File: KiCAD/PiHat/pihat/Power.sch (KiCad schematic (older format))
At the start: 0 parts

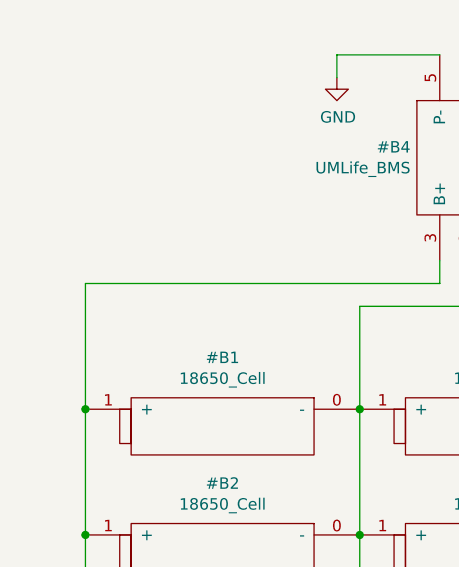
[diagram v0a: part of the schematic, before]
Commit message: Added status LEDs, power relay, organized traces
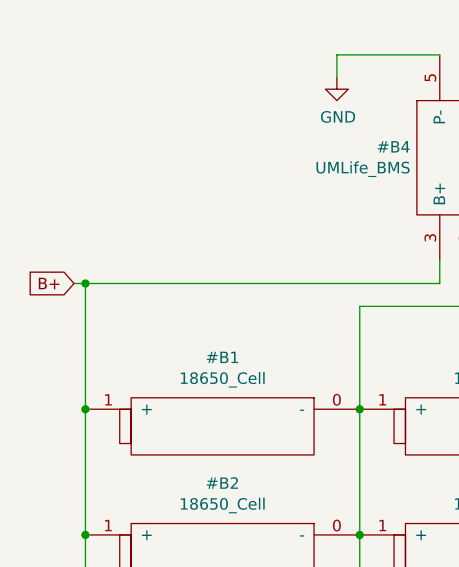
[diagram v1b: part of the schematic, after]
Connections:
- net labels added: B+
- wire segments 34 -> 35
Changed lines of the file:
@@
 EESchema Schematic File Version 4
-LIBS:pihat-cache
 EELAYER 30 0
 EELAYER END
@@
 $EndComp
 $Comp
+L Device:Solar_Cell #SC1
+U 1 1 5E5BBB14
+P 4550 3850
+F 0 "#SC1" H 4383 3946 50  0000 R CNN
+F 1 "Solar_Cell" H 4383 3855 50  0000 R CNN
+F 2 "" V 4550 3910 50  0001 C CNN
+F 3 "~" V 4550 3910 50  0001 C CNN
+	1    4550 3850
+	1    0    0    -1
+$EndComp
+$Comp
+L power:GND #PWR011
+U 1 1 5E5BEAFD
+P 4550 4250
+F 0 "#PWR011" H 4550 4000 50  0001 C CNN
+F 1 "GND" H 4555 4077 50  0000 C CNN
+F 2 "" H 4550 4250 50  0001 C CNN
+F 3 "" H 4550 4250 50  0001 C CNN
+	1    4550 4250
+	1    0    0    -1
+$EndComp
+Wire Wire Line
+	4550 3950 4550 4250
+$Comp
+L Diode:1N4001 #D1
+U 1 1 5E5C0244
+P 4100 3500
+F 0 "#D1" H 4100 3716 50  0000 C CNN
+F 1 "1N4001" H 4100 3625 50  0000 C CNN
+F 2 "Diode_THT:D_DO-41_SOD81_P10.16mm_Horizontal" H 4100 3325 50  0001 C CNN
+F 3 "http://www.vishay.com/docs/88503/1n4001.pdf" H 4100 3500 50  0001 C CNN
+	1    4100 3500
+	1    0    0    -1
+$EndComp
+Wire Wire Line
+	4550 3650 4550 3500
+Wire Wire Line
+	4550 3500 4250 3500
+Wire Wire Line
+	3200 4150 3200 3500
+Wire Wire Line
+	3200 3500 3950 3500
+Wire Wire Line
+	3200 3500 3200 2950
+Connection ~ 3200 3500
+$Comp
+L Connector:Jack-DC #J1
+U 1 1 5E5C5C29
+P 1450 3050
+F 0 "#J1" H 1507 3375 50  0000 C CNN
+F 1 "Jack-DC" H 1507 3284 50  0000 C CNN
+F 2 "" H 1500 3010 50  0001 C CNN
+F 3 "~" H 1500 3010 50  0001 C CNN
+	1    1450 3050
+	1    0    0    -1
+$EndComp
+$Comp
+L power:GND #PWR08
+U 1 1 5E5C81BC
+P 1900 3350
+F 0 "#PWR08" H 1900 3100 50  0001 C CNN
+F 1 "GND" H 1905 3177 50  0000 C CNN
+F 2 "" H 1900 3350 50  0001 C CNN
+F 3 "" H 1900 3350 50  0001 C CNN
+	1    1900 3350
+	1    0    0    -1
+$EndComp
+Wire Wire Line
+	1750 3150 1900 3150
+Wire Wire Line
+	1900 3150 1900 3350
+Wire Wire Line
+	1750 2950 3200 2950
+Wire Wire Line
+	3200 2950 3200 2350
+Connection ~ 3200 2950
+$Comp
+L power:GND #PWR010
+U 1 1 5E5D113A
+P 3450 2500
+F 0 "#PWR010" H 3450 2250 50  0001 C CNN
+F 1 "GND" H 3455 2327 50  0000 C CNN
+F 2 "" H 3450 2500 50  0001 C CNN
+F 3 "" H 3450 2500 50  0001 C CNN
+	1    3450 2500
+	1    0    0    -1
+$EndComp
+Wire Wire Line
+	3450 2500 3450 2350
+Text GLabel 3250 2300 0    50   Input ~ 0
+Pi_Power_+
+Text GLabel 3400 2300 2    50   Input ~ 0
+Pi_Power_-
+Wire Wire Line
+	2250 4150 2250 4250
+Wire Wire Line
+	2700 4150 2250 4150
+$Comp
 L power:GND #PWR09
 U 1 1 5E5AB8F6
@@
 	1    0    0    -1
 $EndComp
-Wire Wire Line
-	2700 4150 2250 4150
-Wire Wire Line
-	2250 4150 2250 4250
-$Comp
-L Device:Solar_Cell #SC1
-U 1 1 5E5BBB14
-P 4550 3850
-F 0 "#SC1" H 4383 3946 50  0000 R CNN
-F 1 "Solar_Cell" H 4383 3855 50  0000 R CNN
-F 2 "" V 4550 3910 50  0001 C CNN
-F 3 "~" V 4550 3910 50  0001 C CNN
-	1    4550 3850
-	1    0    0    -1
-$EndComp
-$Comp
-L power:GND #PWR011
-U 1 1 5E5BEAFD
-P 4550 4250
-F 0 "#PWR011" H 4550 4000 50  0001 C CNN
-F 1 "GND" H 4555 4077 50  0000 C CNN
-F 2 "" H 4550 4250 50  0001 C CNN
-F 3 "" H 4550 4250 50  0001 C CNN
-	1    4550 4250
-	1    0    0    -1
-$EndComp
-Wire Wire Line
-	4550 3950 4550 4250
-$Comp
-L Diode:1N4001 #D1
-U 1 1 5E5C0244
-P 4100 3500
-F 0 "#D1" H 4100 3716 50  0000 C CNN
-F 1 "1N4001" H 4100 3625 50  0000 C CNN
-F 2 "Diode_THT:D_DO-41_SOD81_P10.16mm_Horizontal" H 4100 3325 50  0001 C CNN
-F 3 "http://www.vishay.com/docs/88503/1n4001.pdf" H 4100 3500 50  0001 C CNN
-	1    4100 3500
-	1    0    0    -1
-$EndComp
-Wire Wire Line
-	4550 3650 4550 3500
-Wire Wire Line
-	4550 3500 4250 3500
-Wire Wire Line
-	3200 4150 3200 3500
-Wire Wire Line
-	3200 3500 3950 3500
-Wire Wire Line
-	3200 3500 3200 2950
-Connection ~ 3200 3500
-$Comp
-L Connector:Jack-DC #J1
-U 1 1 5E5C5C29
-P 1450 3050
-F 0 "#J1" H 1507 3375 50  0000 C CNN
-F 1 "Jack-DC" H 1507 3284 50  0000 C CNN
-F 2 "" H 1500 3010 50  0001 C CNN
-F 3 "~" H 1500 3010 50  0001 C CNN
-	1    1450 3050
-	1    0    0    -1
-$EndComp
-$Comp
-L power:GND #PWR08
-U 1 1 5E5C81BC
-P 1900 3350
-F 0 "#PWR08" H 1900 3100 50  0001 C CNN
-F 1 "GND" H 1905 3177 50  0000 C CNN
-F 2 "" H 1900 3350 50  0001 C CNN
-F 3 "" H 1900 3350 50  0001 C CNN
-	1    1900 3350
-	1    0    0    -1
-$EndComp
-Wire Wire Line
-	1750 3150 1900 3150
-Wire Wire Line
-	1900 3150 1900 3350
-Wire Wire Line
-	1750 2950 3200 2950
-Wire Wire Line
-	3200 2950 3200 2350
-Connection ~ 3200 2950
-$Comp
-L power:GND #PWR010
-U 1 1 5E5D113A
-P 3450 2500
-F 0 "#PWR010" H 3450 2250 50  0001 C CNN
-F 1 "GND" H 3455 2327 50  0000 C CNN
-F 2 "" H 3450 2500 50  0001 C CNN
-F 3 "" H 3450 2500 50  0001 C CNN
-	1    3450 2500
-	1    0    0    -1
-$EndComp
-Wire Wire Line
-	3450 2500 3450 2350
-Text GLabel 3250 2300 0    50   Input ~ 0
-Pi_Power_+
-Text GLabel 3400 2300 2    50   Input ~ 0
-Pi_Power_-
+Text GLabel 1100 5150 0    50   Input ~ 0
+B+
+Wire Wire Line
+	1150 5150 1100 5150
+Connection ~ 1150 5150
 $EndSCHEMATC

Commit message: Peer review changes
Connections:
- net labels removed: Pi_Power_-
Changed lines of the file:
@@
 EESchema Schematic File Version 4
+LIBS:pihat-cache
 EELAYER 30 0
 EELAYER END
@@
 Text GLabel 3250 2300 0    50   Input ~ 0
 Pi_Power_+
-Text GLabel 3400 2300 2    50   Input ~ 0
-Pi_Power_-
 Wire Wire Line
 	2250 4150 2250 4250

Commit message: Revision 1
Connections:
- net labels added: +12V, RB085T
- net labels removed: 1N4001, Pi_Power_+
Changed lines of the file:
@@
 EESchema Schematic File Version 4
-LIBS:pihat-cache
 EELAYER 30 0
 EELAYER END
@@
 Wire Wire Line
 	2700 5050 2700 5150
-Wire Wire Line
-	2700 5150 1150 5150
-Wire Wire Line
-	1150 5150 1150 5700
-Connection ~ 1150 5700
 $Comp
 L power:GND #PWR012
@@
 P 4100 3500
 F 0 "#D1" H 4100 3716 50  0000 C CNN
-F 1 "1N4001" H 4100 3625 50  0000 C CNN
+F 1 "RB085T" H 4100 3625 50  0000 C CNN
 F 2 "Diode_THT:D_DO-41_SOD81_P10.16mm_Horizontal" H 4100 3325 50  0001 C CNN
 F 3 "http://www.vishay.com/docs/88503/1n4001.pdf" H 4100 3500 50  0001 C CNN
@@
 Wire Wire Line
 	3200 3500 3950 3500
-Wire Wire Line
-	3200 3500 3200 2950
 Connection ~ 3200 3500
 $Comp
@@
 Wire Wire Line
 	1900 3150 1900 3350
-Wire Wire Line
-	1750 2950 3200 2950
-Wire Wire Line
-	3200 2950 3200 2350
-Connection ~ 3200 2950
 $Comp
 L power:GND #PWR010
@@
 Wire Wire Line
 	3450 2500 3450 2350
-Text GLabel 3250 2300 0    50   Input ~ 0
-Pi_Power_+
 Wire Wire Line
 	2250 4150 2250 4250
@@
 	1    0    0    -1
 $EndComp
-Text GLabel 1100 5150 0    50   Input ~ 0
+Text GLabel 1150 5150 0    50   Input ~ 0
 B+
-Wire Wire Line
-	1150 5150 1100 5150
-Connection ~ 1150 5150
+$Comp
+L Diode:1N4001 #D2
+U 1 1 5E6F2127
+P 2500 2950
+F 0 "#D2" H 2500 3166 50  0000 C CNN
+F 1 "RB085T" H 2500 3075 50  0000 C CNN
+F 2 "Diode_THT:D_DO-41_SOD81_P10.16mm_Horizontal" H 2500 2775 50  0001 C CNN
+F 3 "http://www.vishay.com/docs/88503/1n4001.pdf" H 2500 2950 50  0001 C CNN
+	1    2500 2950
+	-1   0    0    1
+$EndComp
+Wire Wire Line
+	2650 2950 3200 2950
+Connection ~ 3200 2950
+Wire Wire Line
+	3200 2950 3200 3500
+Wire Wire Line
+	2350 2950 1750 2950
+Connection ~ 1150 5700
+Wire Wire Line
+	1150 5150 1150 5700
+Wire Wire Line
+	2700 5150 1150 5150
+Wire Wire Line
+	3200 2350 3200 2950
+$Comp
+L power:+12V #PWR0126
+U 1 1 5E7D68BA
+P 3200 2350
+F 0 "#PWR0126" H 3200 2200 50  0001 C CNN
+F 1 "+12V" H 3215 2523 50  0000 C CNN
+F 2 "" H 3200 2350 50  0001 C CNN
+F 3 "" H 3200 2350 50  0001 C CNN
+	1    3200 2350
+	1    0    0    -1
+$EndComp
 $EndSCHEMATC
